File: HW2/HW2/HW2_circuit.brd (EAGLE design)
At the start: 50 x 50 mm, 23 parts, among them J2 LEFT, J3 RIGHT, X1 MINI-USB_SHIELD5P2-32005-601

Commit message: First Version of Layout
Finished layout with no DRC errors
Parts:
- moved R1 22.5 mm to (6.99, 17.8), turned to 270 degrees
- moved R2 7.96 mm to (15.9, 11.4), turned to 270 degrees
- moved U$5 4.49 mm to (7.62, 3.17), turned to 0 degrees
- moved C7 4.44 mm to (19.7, 10.2), turned to 270 degrees
- moved BUTTON_LED 0.63 mm to (14.6, 2.54), turned to 180 degrees
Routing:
- net +3V3: track 68.0 -> 135.7 mm, vias 2 -> 3
- net B4/USER: track 0.00 -> 37.4 mm
- net D-: track 0.00 -> 36.5 mm, vias 0 -> 3
- net A4/LED: track 0.00 -> 32.7 mm, vias 0 -> 1
- net +5V: track 43.4 -> 73.9 mm, vias 2 -> 3
- net B7: track 0.00 -> 30.5 mm, vias 0 -> 2
- net D+: track 0.00 -> 28.1 mm, vias 0 -> 1
- net USBID: track 0.00 -> 23.0 mm, vias 0 -> 1
- net B8: track 17.1 -> 30.5 mm, vias 1 -> 2
- net VBUS: track 0.00 -> 8.66 mm
- net N$1: track 0.00 -> 4.34 mm

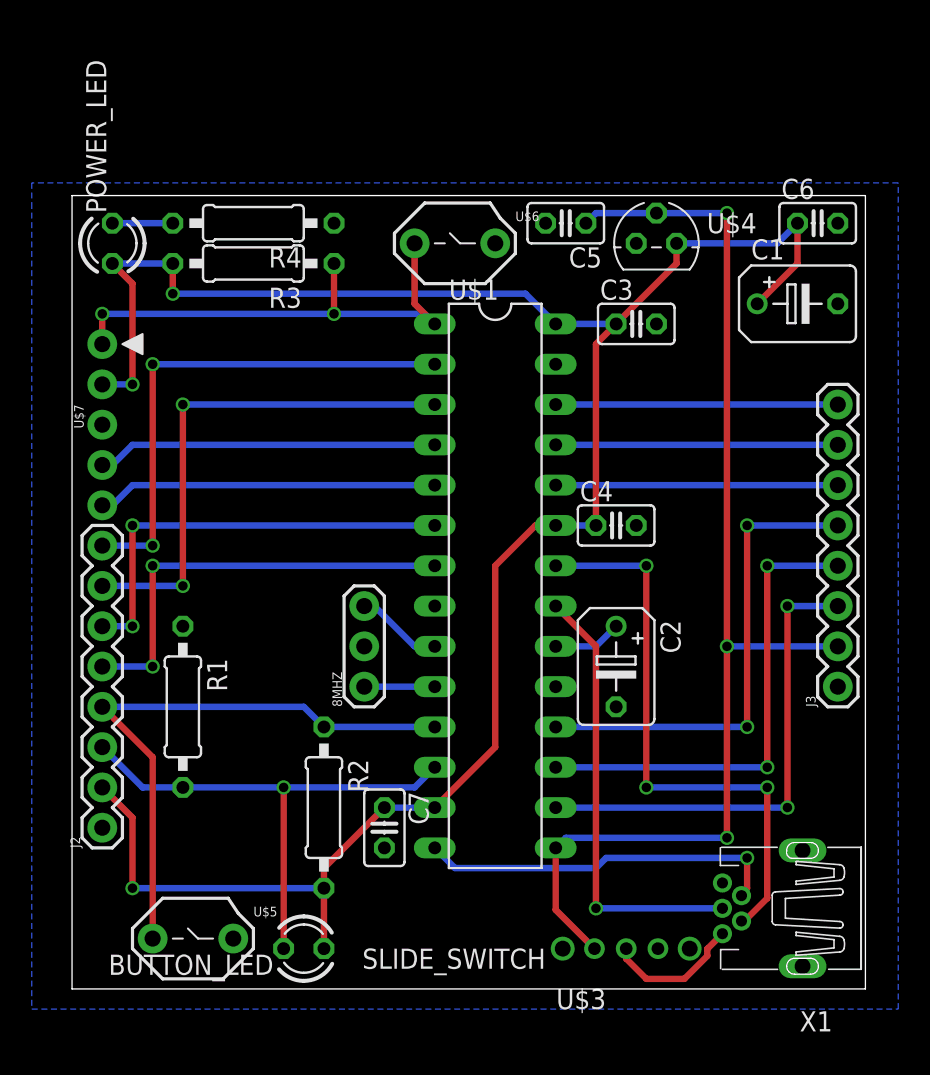
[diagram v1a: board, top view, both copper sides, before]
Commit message: Board Layout Complete
Board layout is finished, passes DRC.  Labels have been added.
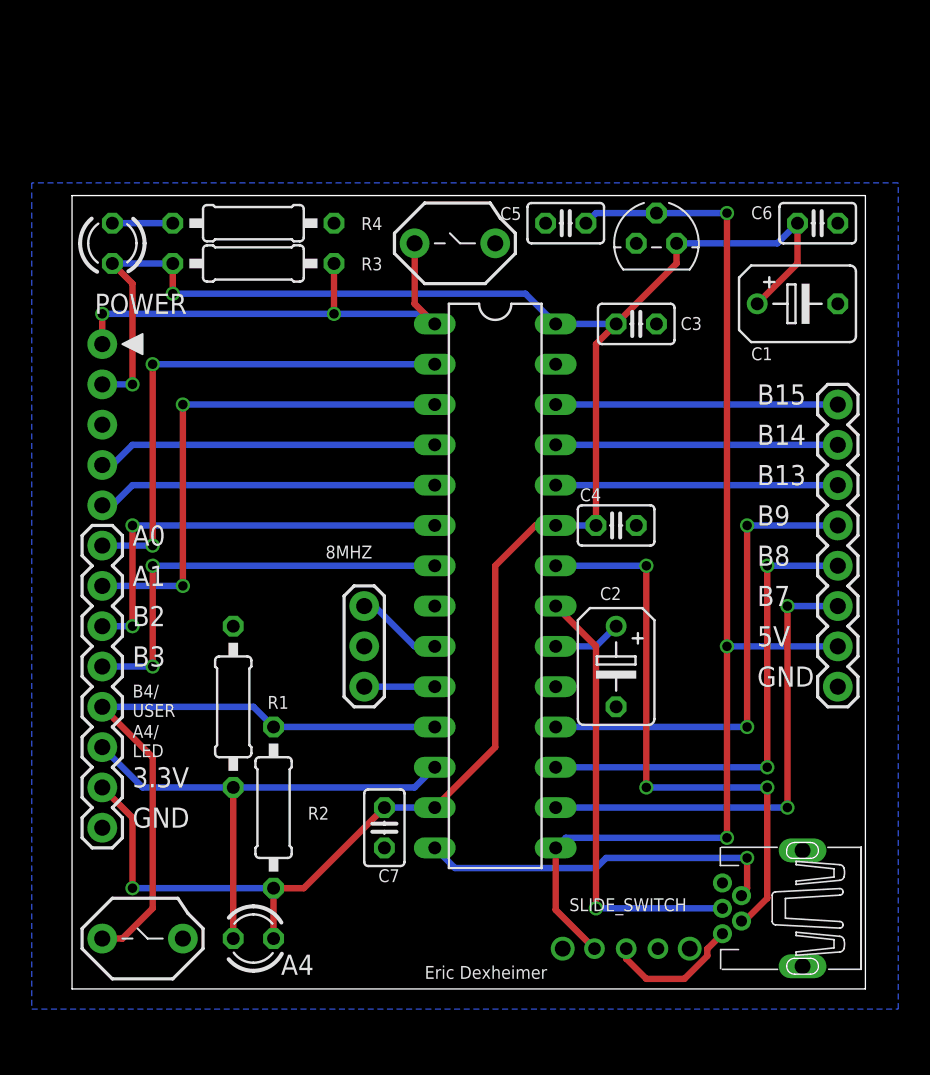
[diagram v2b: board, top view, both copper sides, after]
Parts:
- removed BUTTON_LED: GREEN, ME433:LED3MM
- added A4: A4/LED, ME433:LED3MM
- U$1: value PIC32MX250F128B -> PIC32
- U$7: value PICKIT32 -> PICKIT3
- moved R2 3.18 mm to (12.7, 11.4)
- moved R1 3.17 mm to (10.2, 17.8)
- moved U$5 3.17 mm to (4.45, 3.17)
- renumbered POWER_LED to POWER, U$3 to SLIDE
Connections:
- net +3V3: now also A4.A; no longer BUTTON_LED.A
- net A4/LED: now also A4.K; no longer BUTTON_LED.K
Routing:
- net B4/USER: track 37.4 -> 39.5 mm
- net +3V3: track 135.7 -> 134.3 mm
- net A4/LED: track 32.7 -> 32.1 mm, vias 1 -> 0
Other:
- board text added: "3.3V"
- board text added: "5V"
- board text added: "A0"
- board text added: "A1"
- board text added: "A4/ LED"
- board text added: "B13"
- board text added: "B14"
- board text added: "B15"
- board text added: "B2"
- board text added: "B3"
- board text added: "B4/ USER"
- board text added: "B7"
- board text added: "B8"
- board text added: "B9"
- board text added: "Eric Dexheimer"
- board text added: "GND"

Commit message: Gerber Files and Board
Board silkscreen adjusted and bmp added.  Gerber finals generated.
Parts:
- removed SLIDE: SLIDE_SWITCH, ME433:SLIDE_SWITCH
- added ON: SLIDE_SWITCH, ME433:SLIDE_SWITCH
- U$5: value BUTTON -> USER
- U$6: value BUTTON -> RESET
- moved C6 51.0 mm to (21.0, 4.45), turned to 90 degrees
- moved C5 50.8 mm to (8.89, 2.54), turned to 90 degrees
- moved C1 50.3 mm to (15.2, 3.17), turned to 180 degrees
- moved U$4 45.3 mm to (25.4, 3.17), turned to 180 degrees
- moved POWER 27.9 mm to (30.5, 47.6), turned to 180 degrees
- moved U$6 14.0 mm to (10.2, 47.0)
- moved A4 12.6 mm to (3.17, 12.7), turned to 90 degrees
- moved R4 10.2 mm to (21.6, 48.3), turned to 0 degrees
- moved J2 6.38 mm to (1.27, 16.5)
- moved U$7 6.38 mm to (1.27, 41.9)
- moved R3 4.58 mm to (14.0, 41.9)
- moved R2 2.84 mm to (15.2, 12.7)
- moved C3 2.84 mm to (33.0, 40.6), turned to 270 degrees
- moved J3 2.59 mm to (48.8, 16.5)
- moved R1 2.29 mm to (8.26, 16.5), turned to 90 degrees
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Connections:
- net +5V: now also ON.2; no longer SLIDE.2
- net VBUS: now also ON.3; no longer SLIDE.3
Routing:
- net +5V: track 73.9 -> 52.6 mm, vias 3 -> 0
- net MCLR: track 31.9 -> 23.7 mm, vias 2 -> 0
- net B8: track 30.5 -> 22.5 mm, vias 2 -> 0
- net B9: track 30.5 -> 22.5 mm, vias 2 -> 0
- net B7: track 30.5 -> 22.5 mm, vias 2 -> 0
- net B4/USER: track 39.5 -> 46.0 mm
- net A1: track 32.4 -> 25.9 mm
- net A0: track 32.4 -> 25.9 mm
- net B3: track 27.3 -> 21.6 mm, vias 2 -> 0
- net B2: track 27.3 -> 21.6 mm, vias 2 -> 0
- net PGED1: track 21.5 -> 26.7 mm, vias 0 -> 2
- net PGEC1: track 21.5 -> 26.7 mm, vias 0 -> 2
- net A4/LED: track 32.1 -> 35.1 mm
- net USBID: track 23.0 -> 25.2 mm
- net B15: track 17.8 -> 19.4 mm
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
